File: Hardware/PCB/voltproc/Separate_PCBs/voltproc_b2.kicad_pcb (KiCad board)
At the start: 2 copper layers, 71 x 40 mm, 5 parts, among them J7 Conn_01x13, SW1 SW_DPDT_x2, SW2 SW_DPDT_x2

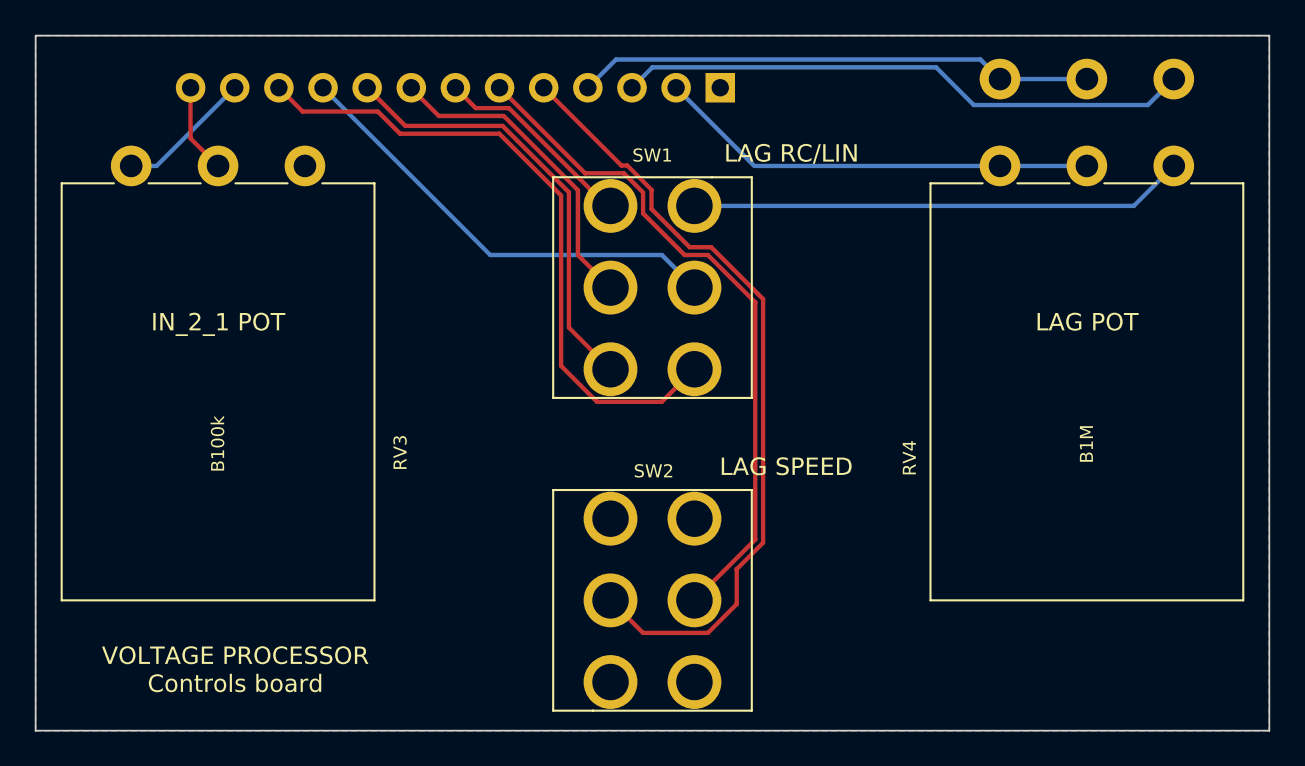
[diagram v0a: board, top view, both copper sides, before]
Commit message: Fix dual pot footprint
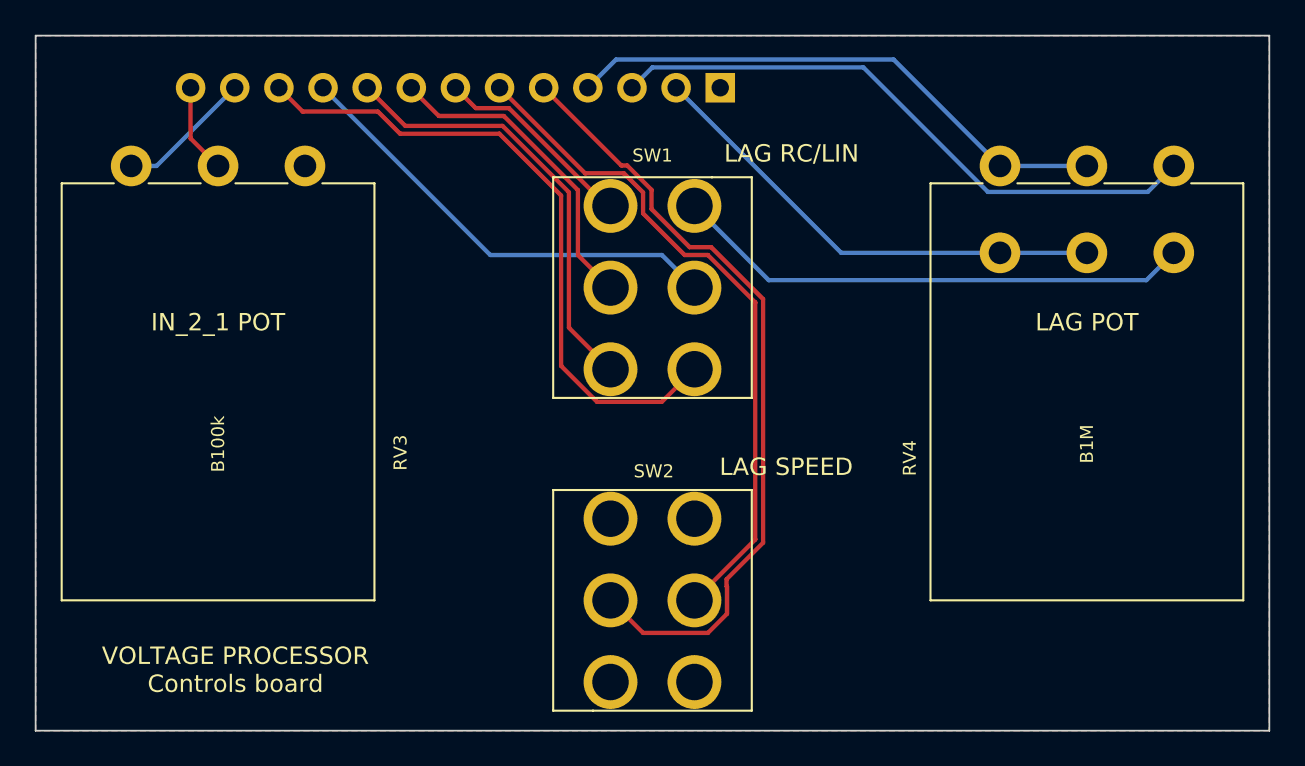
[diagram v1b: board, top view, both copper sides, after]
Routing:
- net Board_0-/Panel components/LAG_LIN_CCW: track 33.2 -> 35.3 mm
- net Board_0-/Panel components/LAG_RC_WIP: track 25.5 -> 27.6 mm
- net Board_0-/Panel components/LAG_LIN_WIP: track 29.9 -> 31.9 mm
- net Board_0-/Panel components/RC_IN: track 28.5 -> 30.0 mm

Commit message: gerbers
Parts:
- added B2: Board, ao_tht:Board_Marker, F.Cu at (50.5, 15.0)
- added GRAF1: Holes, voltproc:voltproc_panel_holes, F.Cu at (50.5, 19.5)
